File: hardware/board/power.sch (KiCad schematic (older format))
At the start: 18 parts, among them J1 Power, SW1 POWER, U1 INA219BxDCN, U2 INA219BxDCN, U3 TLV76733, U4 LM4040-10

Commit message: Re-do the motherboard
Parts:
- removed C1, C4: 4.7uF, Capacitor_SMD:C_0805_2012Metric_Pad1.18x1.45mm_HandSolder, symbol Device:C_Small
- removed C2, C3, C5: 0.1uF, Capacitor_SMD:C_0603_1608Metric_Pad1.08x0.95mm_HandSolder, symbol Device:C_Small
- removed J1: Power, Connector_PinHeader_2.54mm:PinHeader_2x05_P2.54mm_Horizontal, symbol testkit-rescue:Eurorack_Power-winterbloom
- removed U1, U2: INA219BxDCN, Package_TO_SOT_SMD:SOT-23-8, symbol Analog_ADC:INA219BxDCN
- removed U3: TLV76733, winterbloom:TI-DGN-HVSSOP-8_3.0x3.0mm_P0.65mm, symbol winterbloom:TLV76733
- removed U4: LM4040-10, Package_TO_SOT_SMD:SOT-23, symbol winterbloom:LM4040-10
- added C1, C2: 47uF, Capacitor_THT:CP_Radial_D5.0mm_P2.50mm, symbol Device:CP1
- added C3, C4: 10uF, Capacitor_THT:CP_Radial_D5.0mm_P2.50mm, symbol Device:CP1
- added D4: 3.3, winterbloom:LED_0805_Kingbright_APT2012, symbol Device:LED_ALT
- added D5: +12V, winterbloom:LED_0805_Kingbright_APT2012, symbol Device:LED_ALT
- added D6: -12V, winterbloom:LED_0805_Kingbright_APT2012, symbol Device:LED_ALT
- added H1, H2, H3, H4: M3, MountingHole:MountingHole_3.2mm_M3_Pad_Via, symbol Mechanical:MountingHole_Pad
- added J1: POWER, Connector_Wire:SolderWire-0.75sqmm_1x03_P4.8mm_D1.25mm_OD2.3mm, symbol Connector_Generic:Conn_01x03
- added U1: LD1117-3.3, Package_TO_SOT_SMD:SOT-223-3_TabPin2, symbol winterbloom:LM1117-3.3
- D1, D2: value 1N5819 -> BARRIER; footprint Diode_SMD:D_SOD-123 -> winterbloom:DIODE_SOD-123_SOD-123F
- R1, R2: value 1R -> 1k; footprint Resistor_SMD:R_1210_3225Metric_Pad1.30x2.65mm_HandSolder -> Resistor_SMD:R_0603_1608Metric_Pad0.98x0.95mm_HandSolder; mpn RC2010FK-071RL -> (none)
- R3: value 270 -> 1k
- SW1: footprint Connector_PinSocket_2.54mm:PinSocket_2x02_P2.54mm_Vertical -> Connector_Wire:SolderWire-0.75sqmm_1x04_P4.8mm_D1.25mm_OD2.3mm
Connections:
- net +12V: now also R2.1, SW1.3, C3.1, U1.3 (VI)
- net +12VRAW: now also C1.1, J1.3 (Pin_3); no longer R1.1
- net +3V3: now also R1.1, C4.1, U1.2 (VO)
- net -12V: now also SW1.1, D6.1 (K); no longer R3.1
- net -12VRAW: now also C2.2, J1.1 (Pin_1); no longer R2.2
- net GND: now also R3.1, C1.2, C2.1, C3.2, C4.2, D4.1 (K), D5.1 (K), H1.1, H2.1, H3.1, H4.1, J1.2 (Pin_2), U1.1 (GND)
- net +12VMONITORED: no longer names the net of R1.2
- net +12VMONITORED: now also D4.2 (A); no longer SW1.3
- net -10V: no longer names the net of R3.2
- net -10V: now also D6.2 (A)
- removed net -12VMONITORED: R2.1, SW1.1
- new net: D5.2 (A), R2.2
- no-connect marks 1 -> 0
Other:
- note removed: "Maybe raise to 2A?"
- note removed: "TODO: Calculate current requirements"
- moved on the sheet: D1, D2, FB1, FB2, SW1

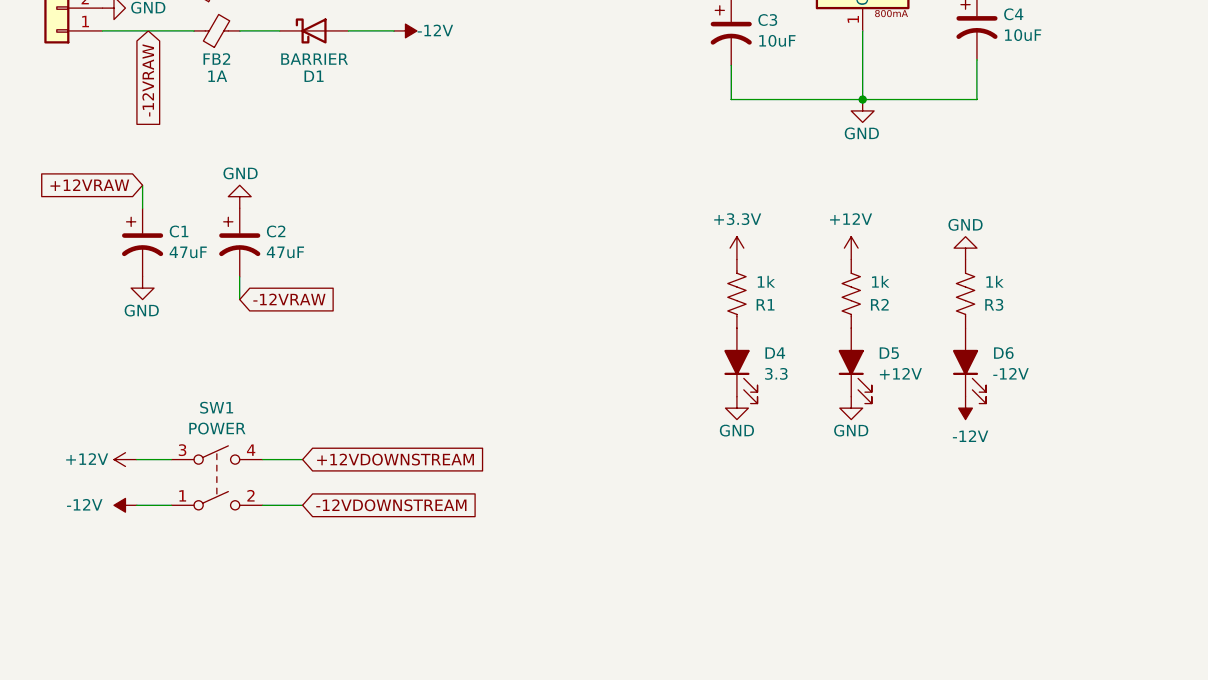
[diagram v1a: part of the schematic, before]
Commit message: Fix issues found in hardware v1
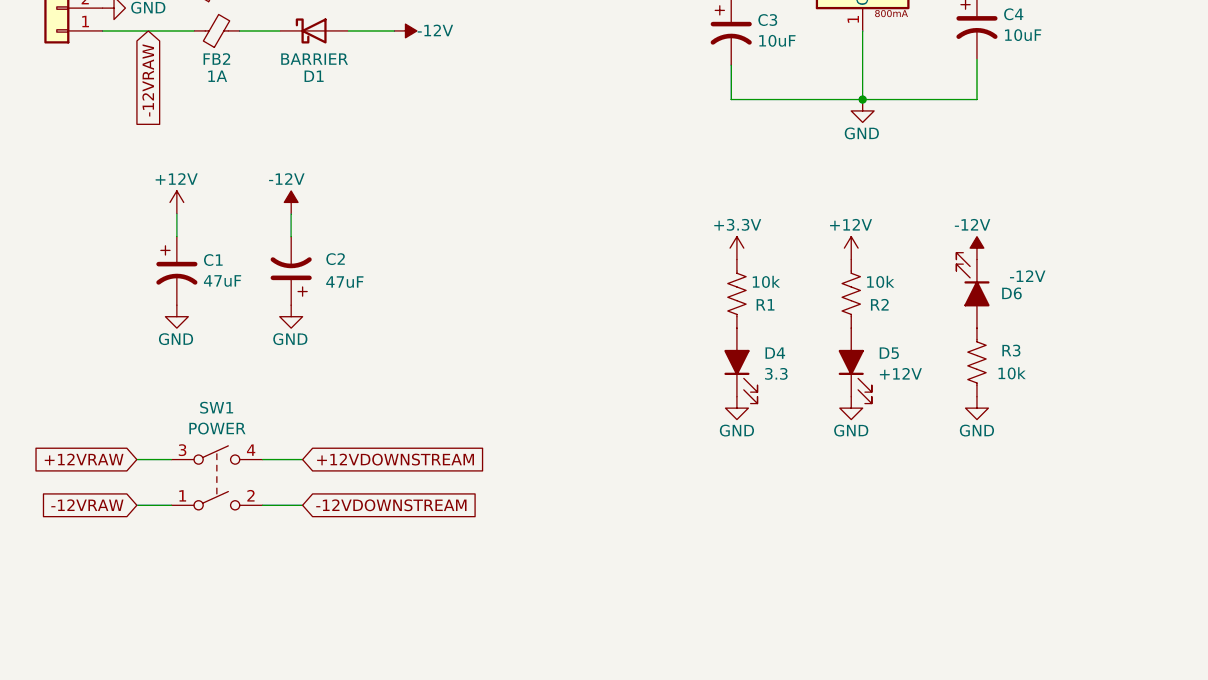
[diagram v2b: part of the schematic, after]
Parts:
- R1, R2, R3: value 1k -> 10k
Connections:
- net +12V: now also C1.1; no longer SW1.3
- net +12VRAW: now also SW1.3; no longer C1.1
- net -12V: now also C2.2; no longer SW1.1
- net -12VRAW: now also SW1.1; no longer C2.2
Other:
- moved on the sheet: C1, C2, D6, R3
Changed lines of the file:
@@
 Sheet 2 7
 Title "TestKit Motherboard"
-Date "2021-10-22"
-Rev "v1"
+Date "2021-11-12"
+Rev "v2"
 Comp "Winterbloom"
 Comment1 "Alethea Flowers"
@@
 Wire Wire Line
 	1500 1050 1700 1050
-$Comp
-L power:+12V #PWR05
-U 1 1 6071F0F9
-P 1075 3125
-F 0 "#PWR05" H 1075 2975 50  0001 C CNN
-F 1 "+12V" V 1075 3250 50  0000 L CNN
-F 2 "" H 1075 3125 50  0001 C CNN
-F 3 "" H 1075 3125 50  0001 C CNN
-	1    1075 3125
-	0    -1   -1   0
-$EndComp
 Wire Wire Line
 	2200 1250 2000 1250
@@
 L Device:CP1 C1
 U 1 1 61721677
-P 1100 2175
-F 0 "C1" H 1215 2221 50  0000 L CNN
-F 1 "47uF" H 1215 2130 50  0000 L CNN
-F 2 "Capacitor_THT:CP_Radial_D5.0mm_P2.50mm" H 1100 2175 50  0001 C CNN
-F 3 "~" H 1100 2175 50  0001 C CNN
-	1    1100 2175
+P 1250 2300
+F 0 "C1" H 1365 2346 50  0000 L CNN
+F 1 "47uF" H 1365 2255 50  0000 L CNN
+F 2 "Capacitor_THT:CP_Radial_D5.0mm_P2.50mm" H 1250 2300 50  0001 C CNN
+F 3 "~" H 1250 2300 50  0001 C CNN
+	1    1250 2300
 	1    0    0    -1
 $EndComp
@@
 L Device:CP1 C2
 U 1 1 61721CD5
-P 1525 2175
-F 0 "C2" H 1640 2221 50  0000 L CNN
-F 1 "47uF" H 1640 2130 50  0000 L CNN
-F 2 "Capacitor_THT:CP_Radial_D5.0mm_P2.50mm" H 1525 2175 50  0001 C CNN
-F 3 "~" H 1525 2175 50  0001 C CNN
-	1    1525 2175
-	1    0    0    -1
+P 1750 2300
+F 0 "C2" H 1600 2250 50  0000 R CNN
+F 1 "47uF" H 1600 2350 50  0000 R CNN
+F 2 "Capacitor_THT:CP_Radial_D5.0mm_P2.50mm" H 1750 2300 50  0001 C CNN
+F 3 "~" H 1750 2300 50  0001 C CNN
+	1    1750 2300
+	-1   0    0    1
 $EndComp
 $Comp
 L power:GND #PWR0115
 U 1 1 61722D1A
-P 1100 2325
-F 0 "#PWR0115" H 1100 2075 50  0001 C CNN
-F 1 "GND" H 1175 2175 50  0000 R CNN
-F 2 "" H 1100 2325 50  0001 C CNN
-F 3 "" H 1100 2325 50  0001 C CNN
-	1    1100 2325
+P 1250 2450
+F 0 "#PWR0115" H 1250 2200 50  0001 C CNN
+F 1 "GND" H 1325 2300 50  0000 R CNN
+F 2 "" H 1250 2450 50  0001 C CNN
+F 3 "" H 1250 2450 50  0001 C CNN
+	1    1250 2450
 	1    0    0    -1
 $EndComp
@@
 L power:GND #PWR0116
 U 1 1 61723462
-P 1525 2025
-F 0 "#PWR0116" H 1525 1775 50  0001 C CNN
-F 1 "GND" H 1600 1875 50  0000 R CNN
-F 2 "" H 1525 2025 50  0001 C CNN
-F 3 "" H 1525 2025 50  0001 C CNN
-	1    1525 2025
-	-1   0    0    1
-$EndComp
-$Comp
-L power:-12V #PWR0117
-U 1 1 61728B98
-P 1075 3325
-F 0 "#PWR0117" H 1075 3425 50  0001 C CNN
-F 1 "-12V" V 1075 3475 50  0000 L CNN
-F 2 "" H 1075 3325 50  0001 C CNN
-F 3 "" H 1075 3325 50  0001 C CNN
-	1    1075 3325
-	0    -1   -1   0
+P 1750 2450
+F 0 "#PWR0116" H 1750 2200 50  0001 C CNN
+F 1 "GND" H 1825 2300 50  0000 R CNN
+F 2 "" H 1750 2450 50  0001 C CNN
+F 3 "" H 1750 2450 50  0001 C CNN
+	1    1750 2450
+	1    0    0    -1
 $EndComp
 $Comp
@@
 AR Path="/60711259/617EC989" Ref="R1"  Part="1"
 F 0 "R1" H 3825 2350 50  0000 C CNN
-F 1 "1k" H 3825 2450 50  0000 C CNN
+F 1 "10k" H 3825 2450 50  0000 C CNN
 F 2 "Resistor_SMD:R_0603_1608Metric_Pad0.98x0.95mm_HandSolder" V 3740 2390 50  0001 C CNN
 F 3 "~" H 3700 2400 50  0001 C CNN
@@
 P 3700 2250
 F 0 "#PWR0120" H 3700 2100 50  0001 C CNN
-F 1 "+3.3V" H 3700 2425 50  0000 C CNN
+F 1 "+3.3V" H 3700 2400 50  0000 C CNN
 F 2 "" H 3700 2250 50  0001 C CNN
 F 3 "" H 3700 2250 50  0001 C CNN
@@
 AR Path="/60711259/617EDA50" Ref="R2"  Part="1"
 F 0 "R2" H 4325 2350 50  0000 C CNN
-F 1 "1k" H 4325 2450 50  0000 C CNN
+F 1 "10k" H 4325 2450 50  0000 C CNN
 F 2 "Resistor_SMD:R_0603_1608Metric_Pad0.98x0.95mm_HandSolder" V 4240 2390 50  0001 C CNN
 F 3 "~" H 4200 2400 50  0001 C CNN
@@
 P 4200 2250
 F 0 "#PWR0136" H 4200 2100 50  0001 C CNN
-F 1 "+12V" H 4100 2425 50  0000 L CNN
+F 1 "+12V" H 4100 2400 50  0000 L CNN
 F 2 "" H 4200 2250 50  0001 C CNN
 F 3 "" H 4200 2250 50  0001 C CNN
@@
 L power:GND #PWR?
 U 1 1 617EE346
-P 4700 2250
+P 4750 2850
 AR Path="/608B4064/617EE346" Ref="#PWR?"  Part="1"
 AR Path="/60711259/617EE346" Ref="#PWR0137"  Part="1"
-F 0 "#PWR0137" H 4700 2000 50  0001 C CNN
-F 1 "GND" H 4700 2100 50  0000 C CNN
-F 2 "" H 4700 2250 50  0001 C CNN
-F 3 "" H 4700 2250 50  0001 C CNN
-	1    4700 2250
-	-1   0    0    1
+F 0 "#PWR0137" H 4750 2600 50  0001 C CNN
+F 1 "GND" H 4750 2700 50  0000 C CNN
+F 2 "" H 4750 2850 50  0001 C CNN
+F 3 "" H 4750 2850 50  0001 C CNN
+	1    4750 2850
+	1    0    0    -1
 $EndComp
 $Comp
 L Device:R_US R?
 U 1 1 617EE33C
-P 4700 2400
+P 4750 2700
 AR Path="/608B4064/617EE33C" Ref="R?"  Part="1"
 AR Path="/60711259/617EE33C" Ref="R3"  Part="1"
-F 0 "R3" H 4825 2350 50  0000 C CNN
-F 1 "1k" H 4825 2450 50  0000 C CNN
-F 2 "Resistor_SMD:R_0603_1608Metric_Pad0.98x0.95mm_HandSolder" V 4740 2390 50  0001 C CNN
-F 3 "~" H 4700 2400 50  0001 C CNN
-	1    4700 2400
-	1    0    0    -1
+F 0 "R3" H 4600 2650 50  0000 C CNN
+F 1 "10k" H 4600 2750 50  0000 C CNN
+F 2 "Resistor_SMD:R_0603_1608Metric_Pad0.98x0.95mm_HandSolder" V 4790 2690 50  0001 C CNN
+F 3 "~" H 4750 2700 50  0001 C CNN
+	1    4750 2700
+	-1   0    0    1
 $EndComp
 $Comp
 L Device:LED_ALT D?
 U 1 1 617EE332
-P 4700 2700
+P 4750 2400
 AR Path="/608B4064/617EE332" Ref="D?"  Part="1"
 AR Path="/60711259/617EE332" Ref="D6"  Part="1"
-F 0 "D6" V 4739 2582 50  0000 R CNN
-F 1 "-12V" V 4648 2582 50  0000 R CNN
-F 2 "winterbloom:LED_0805_Kingbright_APT2012" H 4700 2700 50  0001 C CNN
-F 3 "~" H 4700 2700 50  0001 C CNN
-	1    4700 2700
-	0    -1   -1   0
+F 0 "D6" V 4750 2600 50  0000 R CNN
+F 1 "-12V" V 4675 2700 50  0000 R CNN
+F 2 "winterbloom:LED_0805_Kingbright_APT2012" H 4750 2400 50  0001 C CNN
+F 3 "~" H 4750 2400 50  0001 C CNN
+	1    4750 2400
+	0    1    1    0
 $EndComp
 $Comp
 L power:-12V #PWR0138
 U 1 1 617EF25A
-P 4700 2850
-F 0 "#PWR0138" H 4700 2950 50  0001 C CNN
-F 1 "-12V" H 4600 3025 50  0000 L CNN
-F 2 "" H 4700 2850 50  0001 C CNN
-F 3 "" H 4700 2850 50  0001 C CNN
-	1    4700 2850
-	-1   0    0    1
+P 4750 2250
+F 0 "#PWR0138" H 4750 2350 50  0001 C CNN
+F 1 "-12V" H 4650 2400 50  0000 L CNN
+F 2 "" H 4750 2250 50  0001 C CNN
+F 3 "" H 4750 2250 50  0001 C CNN
+	1    4750 2250
+	1    0    0    -1
 $EndComp
 $Comp
@@
 	-1   0    0    1
 $EndComp
-Text GLabel 1525 2425 2    50   Input ~ 0
--12VRAW
-Wire Wire Line
-	1525 2425 1525 2325
-Text GLabel 1100 1925 0    50   Input ~ 0
-+12VRAW
-Wire Wire Line
-	1100 1925 1100 2025
+Wire Wire Line
+	1750 2050 1750 2150
+Wire Wire Line
+	1250 2050 1250 2150
 $Comp
 L Mechanical:MountingHole_Pad H1
@@
 	1    0    0    -1
 $EndComp
+Text GLabel 1075 3325 0    50   Input ~ 0
+-12VRAW
+Text GLabel 1075 3125 0    50   Input ~ 0
++12VRAW
+$Comp
+L power:+12V #PWR0117
+U 1 1 617F4C4D
+P 1250 2050
+F 0 "#PWR0117" H 1250 1900 50  0001 C CNN
+F 1 "+12V" H 1150 2200 50  0000 L CNN
+F 2 "" H 1250 2050 50  0001 C CNN
+F 3 "" H 1250 2050 50  0001 C CNN
+	1    1250 2050
+	1    0    0    -1
+$EndComp
+$Comp
+L power:-12V #PWR0218
+U 1 1 617F5561
+P 1750 2050
+F 0 "#PWR0218" H 1750 2150 50  0001 C CNN
+F 1 "-12V" H 1650 2200 50  0000 L CNN
+F 2 "" H 1750 2050 50  0001 C CNN
+F 3 "" H 1750 2050 50  0001 C CNN
+	1    1750 2050
+	1    0    0    -1
+$EndComp
